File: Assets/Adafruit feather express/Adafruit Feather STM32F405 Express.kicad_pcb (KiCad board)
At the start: 2 copper layers, 50.8 x 22.9 mm, 63 parts, among them Q3 DMG3405, SW1 KMR2, U1 25Q16, U2 AP2112-3.3, U3 MCP73831T-2ACI/OT, X1 JSTPH, X2 32.768, Y1 12mhz

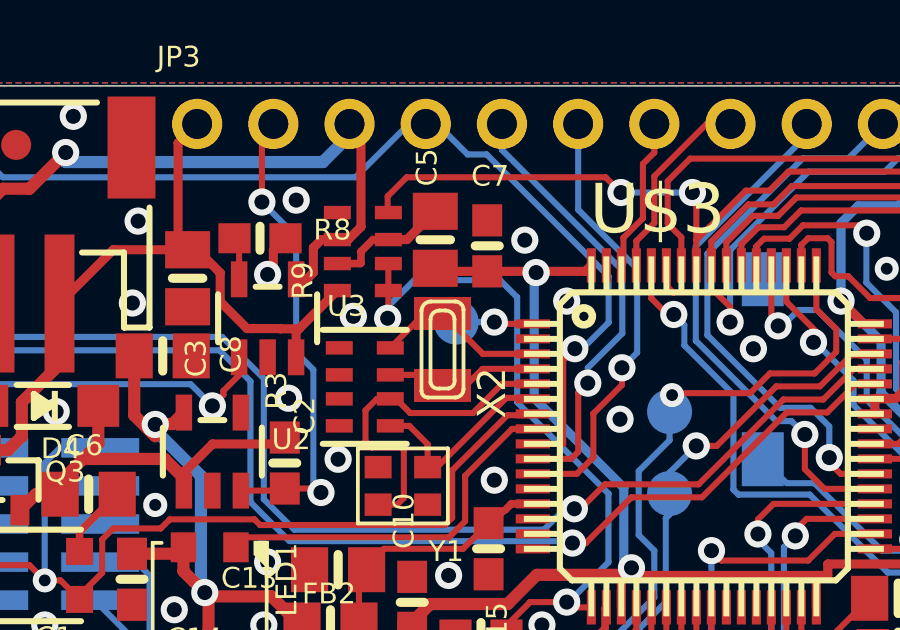
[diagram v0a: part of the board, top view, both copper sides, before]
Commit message: switching from development board to on board chip
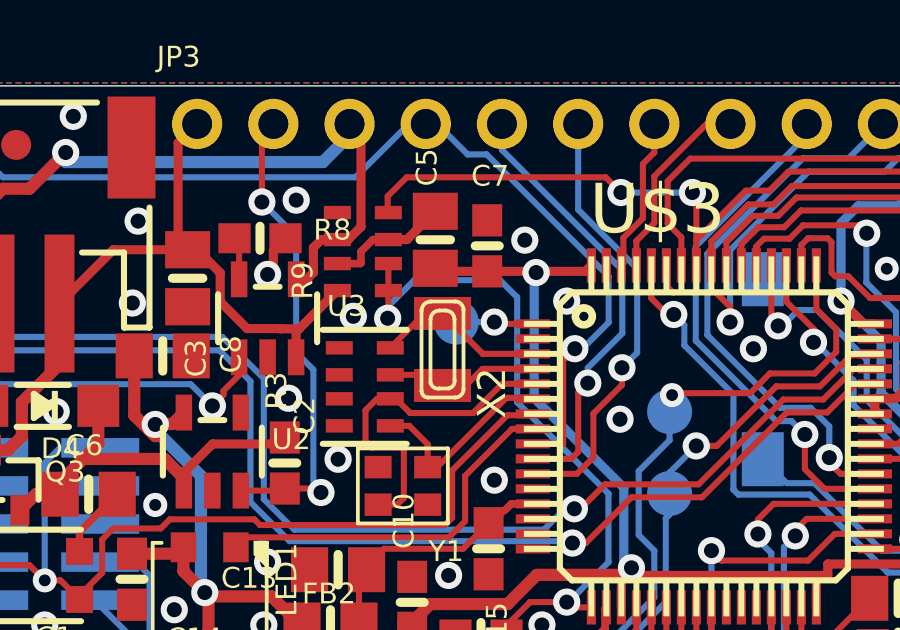
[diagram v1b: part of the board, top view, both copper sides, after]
